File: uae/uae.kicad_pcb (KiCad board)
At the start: 2 copper layers, 45 x 30 mm, 19 parts

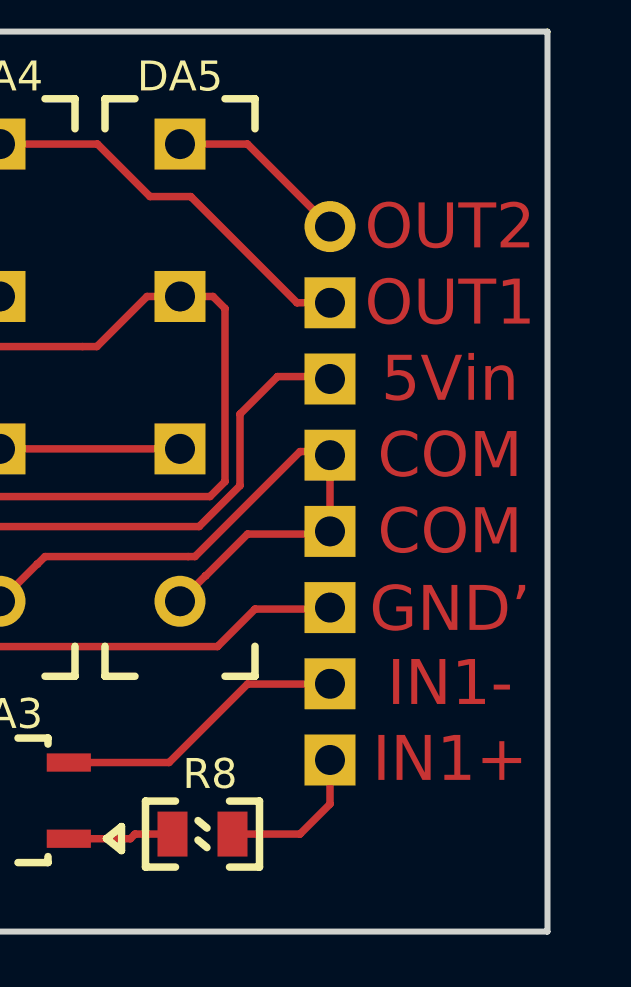
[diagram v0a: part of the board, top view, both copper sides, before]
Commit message: уменьшен зазор паяльной маски, заменены герберы
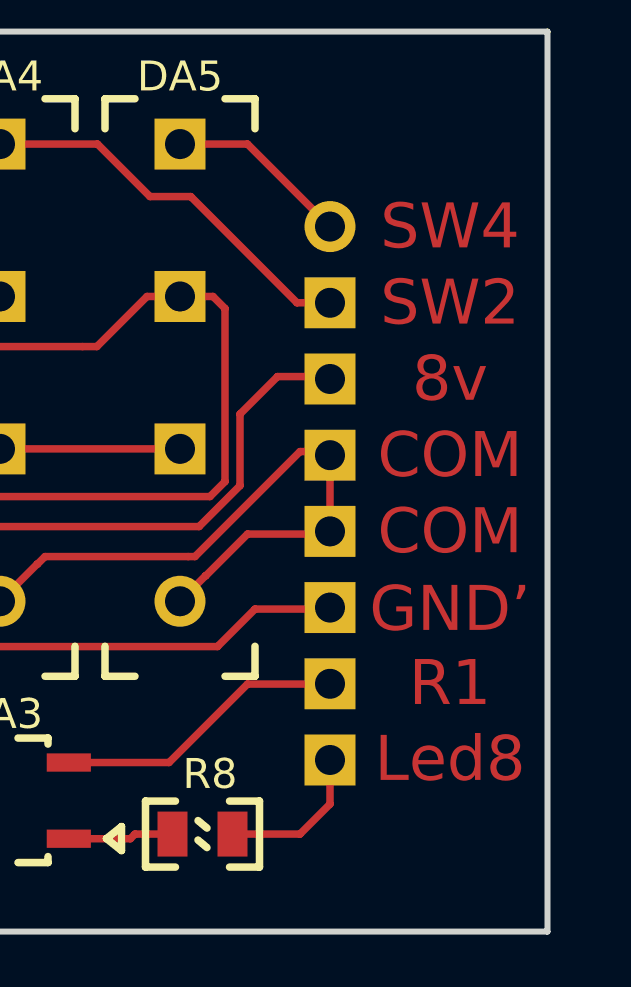
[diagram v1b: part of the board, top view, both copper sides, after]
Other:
- rule pad_to_mask_clearance: 0.2 -> 0.05
- board text added: "8v"
- board text added: "Led8"
- board text added: "R1"
- board text added: "SW2"
- board text added: "SW4"
- board text removed: "5Vin"
- board text removed: "IN1+"
- board text removed: "IN1-"
- board text removed: "OUT1"
- board text removed: "OUT2"
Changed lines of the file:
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@@
     (pad_size 1.524 1.524)
     (pad_drill 0.762)
-    (pad_to_mask_clearance 0.2)
+    (pad_to_mask_clearance 0.05)
+    (solder_mask_min_width 0.2)
     (aux_axis_origin 0 0)
     (visible_elements FFFFFF7F)
     (pcbplotparams
-      (layerselection 0x010fc_ffffffff)
+      (layerselection 0x010f0_ffffffff)
       (usegerberextensions false)
       (usegerberattributes false)
@@
       (outputformat 1)
       (mirror false)
-      (drillshape 1)
+      (drillshape 0)
       (scaleselection 1)
       (outputdirectory ""))
@@
   (gr_line (start 124.75 47.5) (end 124.75 77.5) (layer Edge.Cuts) (width 0.2))
   (gr_line (start 79.75 47.5) (end 124.75 47.5) (layer Edge.Cuts) (width 0.2))
-  (gr_text IN1- (at 121.5 69.22) (layer F.Cu)
+  (gr_text R1 (at 121.5 69.22) (layer F.Cu)
     (effects (font (size 1.5 1.5) (thickness 0.3)))
   )
@@
     (effects (font (size 1.5 1.5) (thickness 0.3)))
   )
-  (gr_text IN1+ (at 121.5 71.75) (layer F.Cu)
+  (gr_text Led8 (at 121.5 71.75) (layer F.Cu)
     (effects (font (size 1.5 1.5) (thickness 0.3)))
   )
@@
     (effects (font (size 1.5 1.5) (thickness 0.3)))
   )
-  (gr_text 5Vin (at 121.5 59.08) (layer F.Cu)
-    (effects (font (size 1.5 1.5) (thickness 0.3)))
-  )
-  (gr_text OUT1 (at 121.5 56.54) (layer F.Cu)
-    (effects (font (size 1.5 1.5) (thickness 0.3)))
-  )
-  (gr_text OUT2 (at 121.5 54) (layer F.Cu)
-    (effects (font (size 1.5 1.5) (thickness 0.3)))
-  )
+  (gr_text 8v (at 121.5 59.08) (layer F.Cu)
+    (effects (font (size 1.5 1.5) (thickness 0.3)))
+  )
+  (gr_text SW2 (at 121.5 56.54) (layer F.Cu)
+    (effects (font (size 1.5 1.5) (thickness 0.3)))
+  )
+  (gr_text SW4 (at 121.5 54) (layer F.Cu)
+    (effects (font (size 1.5 1.5) (thickness 0.3)))
+  )
